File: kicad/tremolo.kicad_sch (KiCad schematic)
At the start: 25 parts, among them IC2 TL072CP

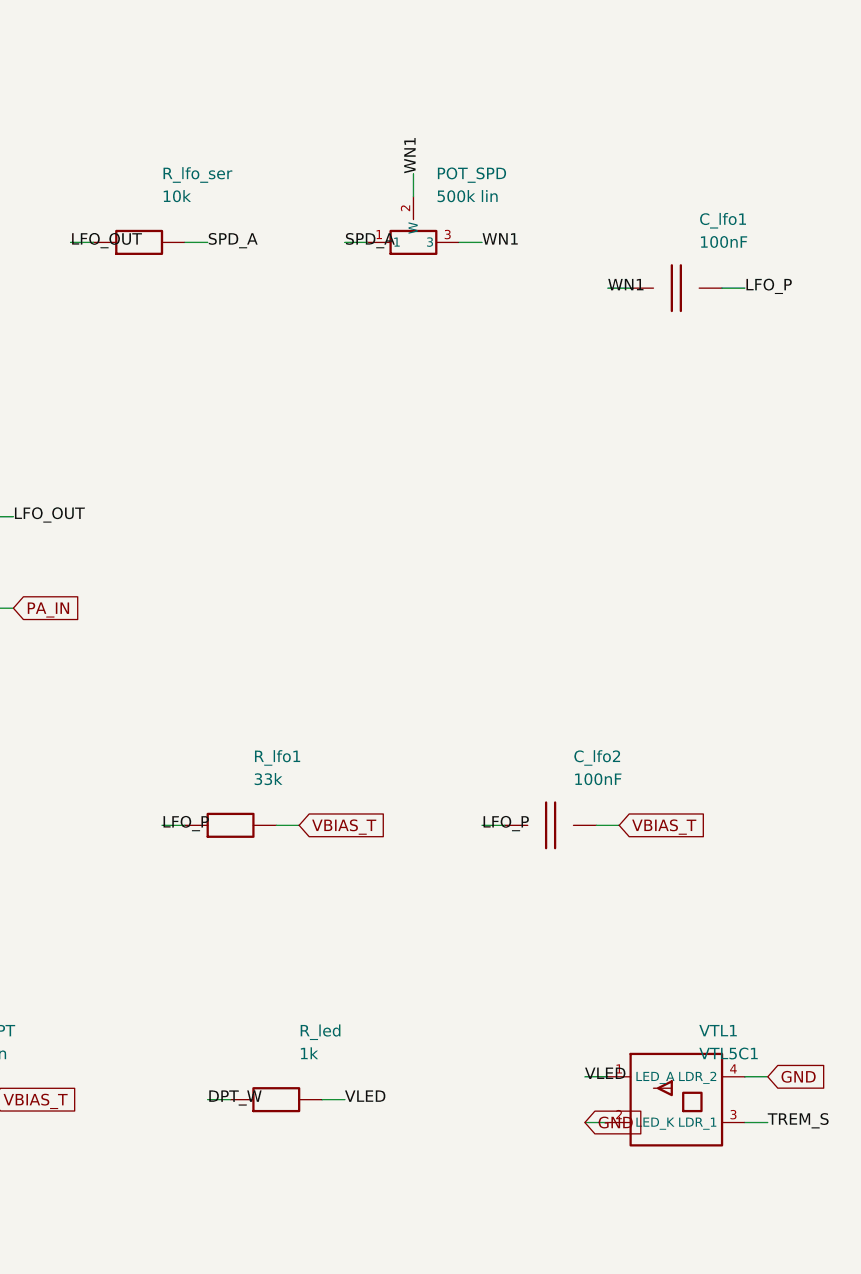
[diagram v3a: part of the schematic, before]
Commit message: SPICE parameter sweeps with committed results; tremolo LFO fix (errata #19); re-route
spice/: six ngspice sweeps next to the fixed-point checks, and run_all.sh now
saves every result table to spice/results/ (committed evidence):
- sweep_preamp_bias: Vd vs R_s for LO/TYP/HI JFET corners (datasheet Idss 1/3/5
  mA). The recovered 2.2k suits a HIGH-Idss part (8.8 V); a typical part wants
  ~1.0k (8.5 V); a 1 mA part cannot reach 8-9 V at any R_s -> errata #15 quantified
- sweep_tonestack: response over the whole pot travel (1 kHz -1.6..-3.3 dB while
  10 kHz falls 14 dB)
- sweep_lfo_speed_recovered: the recovered single-arm Wien LFO oscillates only for
  pot <= ~27k (5 % of travel) at 45-80 Hz, and not at all elsewhere
- sweep_lfo_speed: the fixed network, 10.6 Hz .. 0.60 Hz at constant 0.96 Vpp
- sweep_classa_bias: standing current / heat / THD vs bias (1.4 % -> 0.002 %,
  0.11 -> 0.85 A)
- sweep_pa_headroom: clean power vs rail, mains -10 %..+10 % = 8.9 / 11.7 / 14.8 W

Errata #19 (HIGH): the tremolo LFO did not work as recovered (Wien start condition
gain > 2 + R1/R2 fails with the speed pot in one arm). Built design: dual-gang
250k lin speed pot (one gang per arm, same panel hole), 15k floors, 1 uF timing
caps; POT_SPD_A/B in schematic + BOM = one part. tran_tremolo_lfo.cir aligned
(10.59 Hz at the fast end). Docs: errata, Part 1 s5, Part 2 note, Part 6b, BOM
cross-check, spice README (sweep tables), PCB-NOTES test-point row, README.

Both boards regenerated and re-routed (six settings each; Freerouting is
deterministic per input but placement-sensitive): THT 167/168, 3 starved-thermal
errors (was 166/166 clean); SMD 162/169, DRC clean (was 165/167 + 1 error).
Reports in kicad/reports/, open links listed in PCB-NOTES.

Co-Authored-By: Claude Fable 5.1 <noreply@anthropic.com>
Claude-Session: https://claude.ai/code/session_01Vk8HkvCugxFpQsBPVnNT2H
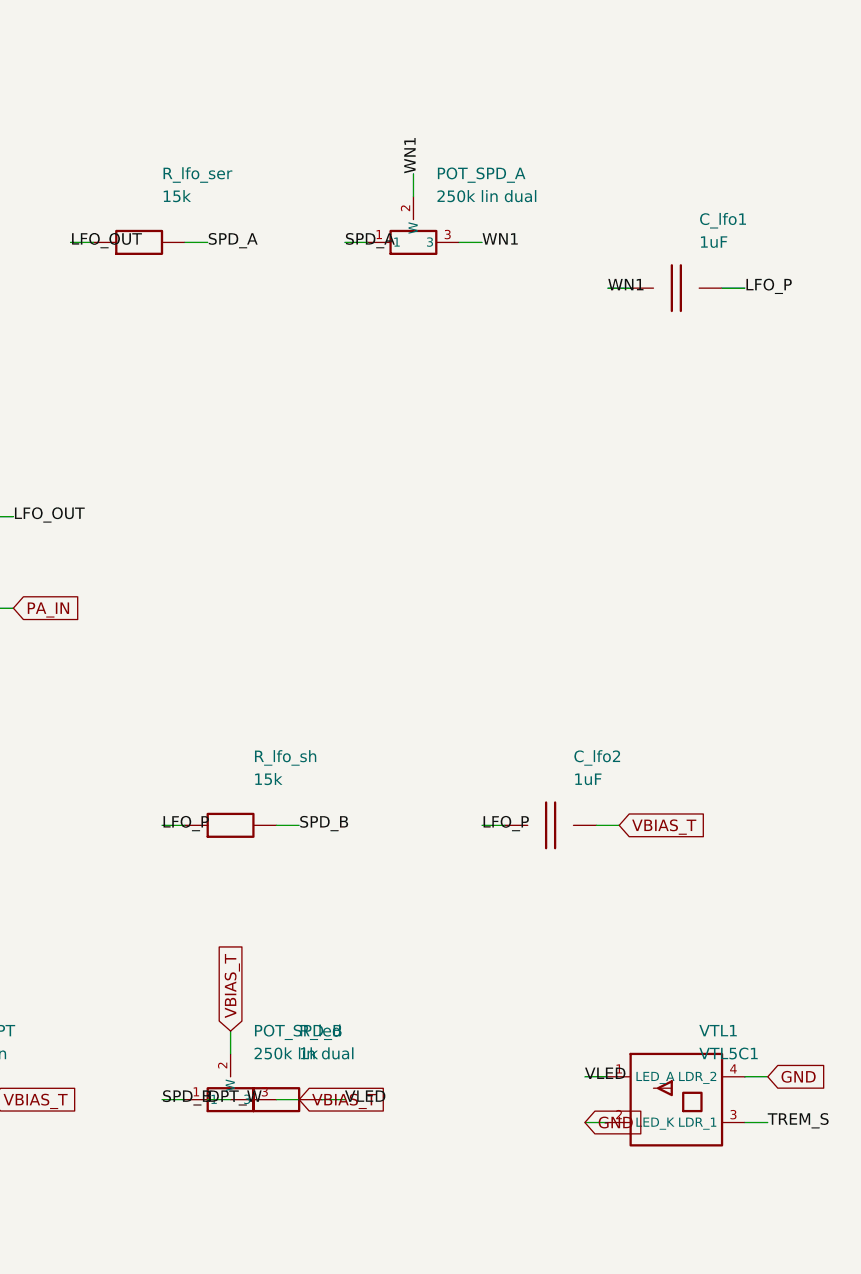
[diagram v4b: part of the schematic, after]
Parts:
- removed POT_SPD: 500k lin, cambridge_reverb:WirePad_1x03_P2.54mm_D1.2mm, symbol cr_primitives:POT
- removed R_lfo1: 33k, Resistor_THT:R_Axial_DIN0207_L6.3mm_D2.5mm_P5.08mm_Vertical, symbol cr_primitives:R
- added POT_SPD_A, POT_SPD_B: 250k lin dual, cambridge_reverb:WirePad_1x03_P2.54mm_D1.2mm, symbol cr_primitives:POT
- added R_lfo_sh: 15k, Resistor_THT:R_Axial_DIN0207_L6.3mm_D2.5mm_P5.08mm_Vertical, symbol cr_primitives:R
- C_lfo1, C_lfo2: value 100nF -> 1uF
- R_lfo_ser: value 10k -> 15k
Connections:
- net LFO_P: now also R_lfo_sh.1
- net SPD_A: now also POT_SPD_A.1
- net VBIAS_T: now also POT_SPD_B.2 (W), POT_SPD_B.3
- net WN1: now also POT_SPD_A.2 (W), POT_SPD_A.3
- new net SPD_B: POT_SPD_B.1, R_lfo_sh.2
